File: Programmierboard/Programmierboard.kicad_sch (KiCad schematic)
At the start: 37 parts, among them J1 Conn_01x10_Socket, J2 Conn_01x10_Socket, J3 Conn_01x10_Socket, J4 Conn_01x10_Socket, J5 DE9_Plug_MountingHoles, J6 Conn_01x10_Socket, J7 Conn_01x10_Socket, Q1 BC327, Q2 BC327, SW1 SW_SPDT, U1 AT89C2051-12P, U2 MAX202, U99 L7805

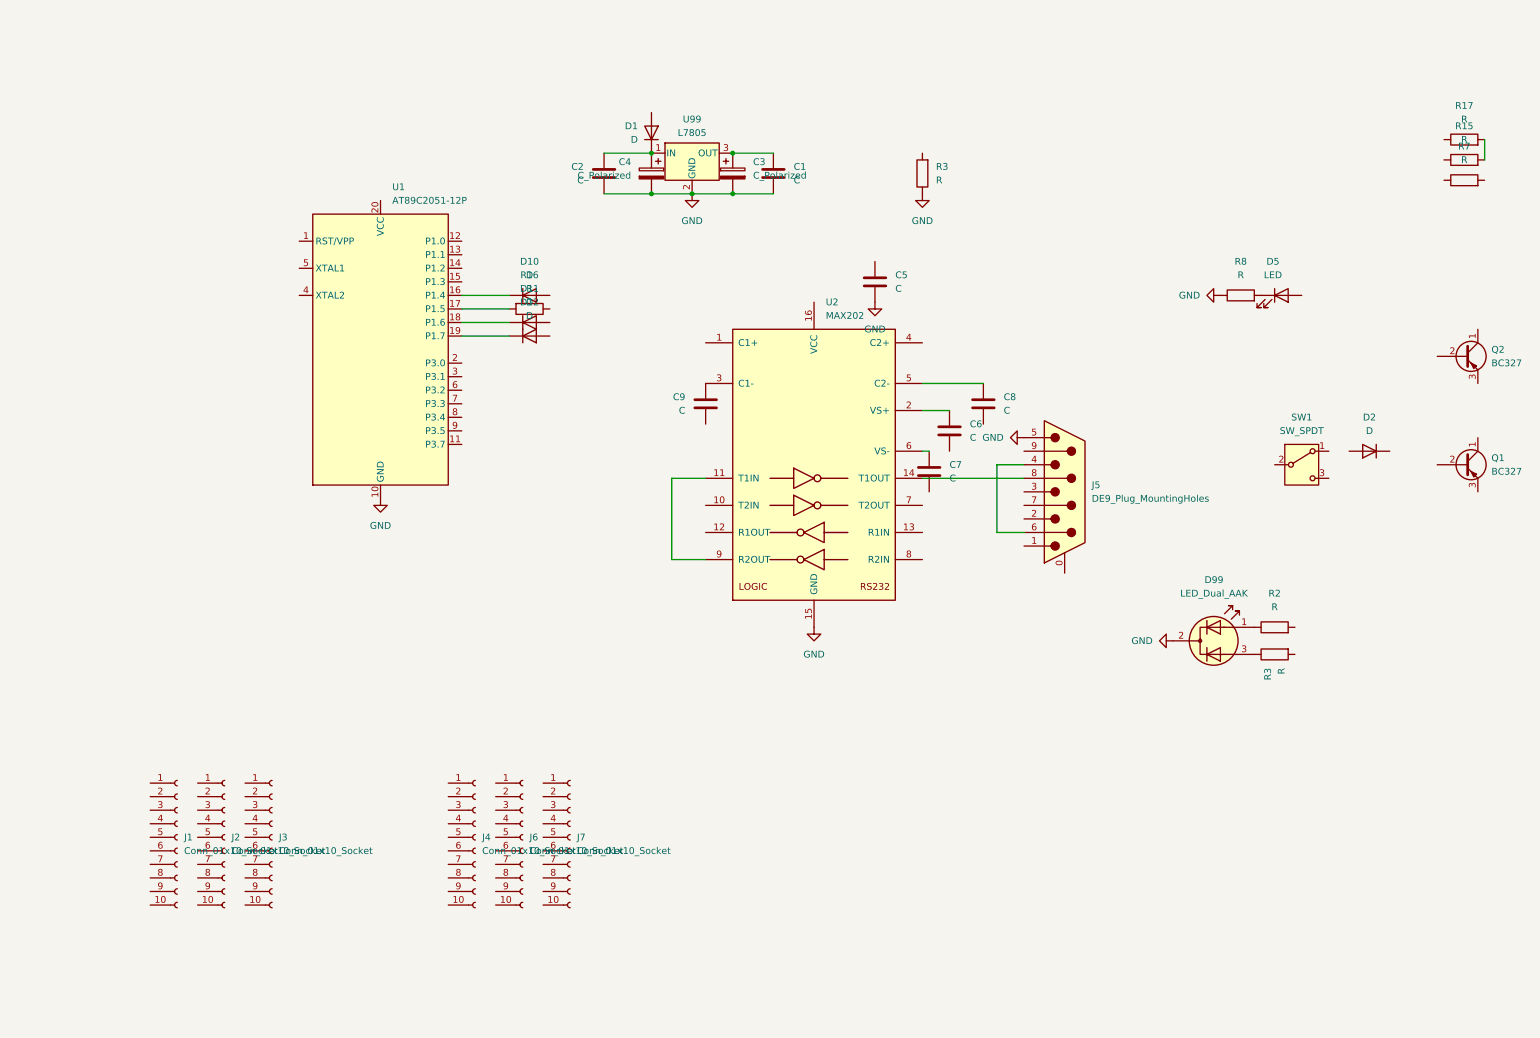
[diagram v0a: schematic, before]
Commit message: footprints und symbole
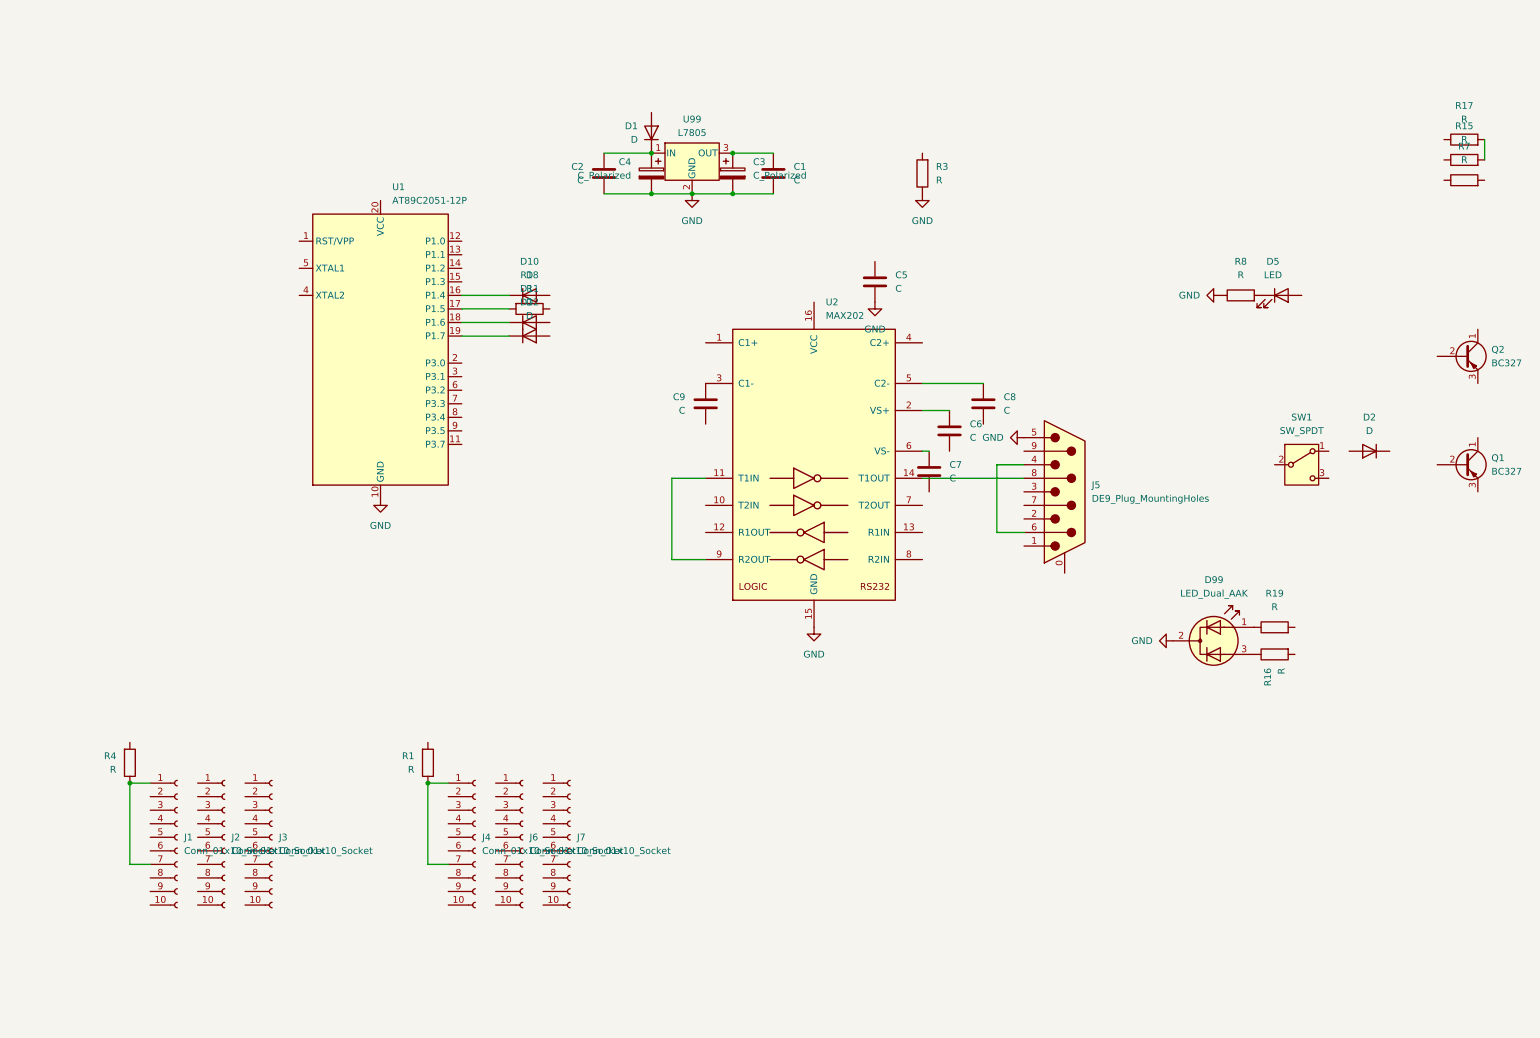
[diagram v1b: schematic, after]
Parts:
- added R1, R4: R, Resistor_THT:R_Axial_DIN0207_L6.3mm_D2.5mm_P10.16mm_Horizontal, symbol Device:R
- renumbered R3 to R16, R16 to R18, R2 to R19
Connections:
- net at J1.1 (Pin_1): now also J1.7 (Pin_7), R4.1
- net at J4.1 (Pin_1): now also J4.7 (Pin_7), R1.1
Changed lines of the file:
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@@
 	)
 	(junction
+		(at 22.86 160.02)
+		(diameter 0)
+		(color 0 0 0 0)
+	)
+	(junction
 		(at 135.89 49.53)
 		(diameter 0)
@@
 	)
 	(junction
+		(at 78.74 160.02)
+		(diameter 0)
+		(color 0 0 0 0)
+	)
+	(junction
 		(at 128.27 49.53)
 		(diameter 0)
@@
 	(wire
 		(pts
+			(xy 22.86 160.02) (xy 26.67 160.02)
+		)
+		(stroke
+			(width 0)
+			(type default)
+		)
+	)
+	(wire
+		(pts
+			(xy 82.55 175.26) (xy 78.74 175.26)
+		)
+		(stroke
+			(width 0)
+			(type default)
+		)
+	)
+	(wire
+		(pts
+			(xy 78.74 175.26) (xy 78.74 160.02)
+		)
+		(stroke
+			(width 0)
+			(type default)
+		)
+	)
+	(wire
+		(pts
 			(xy 124.46 118.11) (xy 124.46 102.87)
 		)
@@
 	(wire
 		(pts
+			(xy 78.74 160.02) (xy 82.55 160.02)
+		)
+		(stroke
+			(width 0)
+			(type default)
+		)
+	)
+	(wire
+		(pts
+			(xy 22.86 175.26) (xy 26.67 175.26)
+		)
+		(stroke
+			(width 0)
+			(type default)
+		)
+	)
+	(wire
+		(pts
 			(xy 85.09 73.66) (xy 93.98 73.66)
 		)
@@
 	(wire
 		(pts
+			(xy 22.86 160.02) (xy 22.86 175.26)
+		)
+		(stroke
+			(width 0)
+			(type default)
+		)
+	)
+	(wire
+		(pts
 			(xy 135.89 49.53) (xy 143.51 49.53)
 		)
@@
 		(dnp no)
 		(fields_autoplaced yes)
-		(property "Reference" "R16"
+		(property "Reference" "R18"
 			(at 97.79 64.77 90)
 			(effects
@@
 			(project "Programmierboard"
 				(path "/7a1d40ec-943a-4f9e-8e53-fdc73602617f"
-					(reference "R16")
+					(reference "R18")
 					(unit 1)
 				)
@@
 	)
 	(symbol
+		(lib_id "Device:R")
+		(at 78.74 156.21 0)
+		(mirror x)
+		(unit 1)
+		(exclude_from_sim no)
+		(in_bom yes)
+		(on_board yes)
+		(dnp no)
+		(property "Reference" "R1"
+			(at 76.2 154.9399 0)
+			(effects
+				(font
+					(size 1.27 1.27)
+				)
+				(justify right)
+			)
+		)
+		(property "Value" "R"
+			(at 76.2 157.4799 0)
+			(effects
+				(font
+					(size 1.27 1.27)
+				)
+				(justify right)
+			)
+		)
+		(property "Footprint" "Resistor_THT:R_Axial_DIN0207_L6.3mm_D2.5mm_P10.16mm_Horizontal"
+			(at 76.962 156.21 90)
+			(effects
+				(font
+					(size 1.27 1.27)
+				)
+				(hide yes)
+			)
+		)
+		(property "Datasheet" "~"
+			(at 78.74 156.21 0)
+			(effects
+				(font
+					(size 1.27 1.27)
+				)
+				(hide yes)
+			)
+		)
+		(property "Description" "Resistor"
+			(at 78.74 156.21 0)
+			(effects
+				(font
+					(size 1.27 1.27)
+				)
+				(hide yes)
+			)
+		)
+		(pin "2"
+		)
+		(pin "1"
+		)
+		(instances
+			(project "Programmierboard"
+				(path "/7a1d40ec-943a-4f9e-8e53-fdc73602617f"
+					(reference "R1")
+					(unit 1)
+				)
+			)
+		)
+	)
+	(symbol
 		(lib_id "Device:C")
 		(at 172.72 101.6 0)
@@
 	)
 	(symbol
+		(lib_id "Device:R")
+		(at 22.86 156.21 0)
+		(mirror x)
+		(unit 1)
+		(exclude_from_sim no)
+		(in_bom yes)
+		(on_board yes)
+		(dnp no)
+		(property "Reference" "R4"
+			(at 20.32 154.9399 0)
+			(effects
+				(font
+					(size 1.27 1.27)
+				)
+				(justify right)
+			)
+		)
+		(property "Value" "R"
+			(at 20.32 157.4799 0)
+			(effects
+				(font
+					(size 1.27 1.27)
+				)
+				(justify right)
+			)
+		)
+		(property "Footprint" "Resistor_THT:R_Axial_DIN0207_L6.3mm_D2.5mm_P10.16mm_Horizontal"
+			(at 21.082 156.21 90)
+			(effects
+				(font
+					(size 1.27 1.27)
+				)
+				(hide yes)
+			)
+		)
+		(property "Datasheet" "~"
+			(at 22.86 156.21 0)
+			(effects
+				(font
+					(size 1.27 1.27)
+				)
+				(hide yes)
+			)
+		)
+		(property "Description" "Resistor"
+			(at 22.86 156.21 0)
+			(effects
+				(font
+					(size 1.27 1.27)
+				)
+				(hide yes)
+			)
+		)
+		(pin "2"
+		)
+		(pin "1"
+		)
+		(instances
+			(project "Programmierboard"
+				(path "/7a1d40ec-943a-4f9e-8e53-fdc73602617f"
+					(reference "R4")
+					(unit 1)
+				)
+			)
+		)
+	)
+	(symbol
 		(lib_id "Transistor_BJT:BC327")
 		(at 273.05 80.01 0)
@@
 		(dnp no)
 		(fields_autoplaced yes)
-		(property "Reference" "R2"
+		(property "Reference" "R19"
 			(at 237.49 124.46 90)
 			(effects
@@
 			(project "Programmierboard"
 				(path "/7a1d40ec-943a-4f9e-8e53-fdc73602617f"
-					(reference "R2")
+					(reference "R19")
 					(unit 1)
 				)
@@
 		(on_board yes)
 		(dnp no)
-		(property "Reference" "R3"
+		(property "Reference" "R16"
 			(at 236.2199 138.43 0)
 			(effects
@@
 			(project "Programmierboard"
 				(path "/7a1d40ec-943a-4f9e-8e53-fdc73602617f"
-					(reference "R3")
+					(reference "R16")
 					(unit 1)
 				)

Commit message: prog
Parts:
- added C10: C, Capacitor_THT:C_Axial_L3.8mm_D2.6mm_P7.50mm_Horizontal, symbol Device:C
- added J8: Conn_01x02_Socket, Connector_PinSocket_2.54mm:PinSocket_1x02_P2.54mm_Vertical, symbol Connector:Conn_01x02_Socket
- D5: value LED -> POWER
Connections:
- net GND: now also C6.2, C7.2, C10.2, J8.2 (Pin_2)
- net VCC: now reaches U1.20 (VCC)
- net VCC: now also C1.1, C3.1, D5.2 (A), R1.2, R15.2, R17.2, U99.3 (OUT), C10.1
- net at J1.1 (Pin_1), J1.7 (Pin_7), R4.1: now also C5.1, J4.1 (Pin_1), J4.7 (Pin_7), R1.1
- new net +12V: J8.1 (Pin_1)
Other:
- moved on the sheet: C5, R17

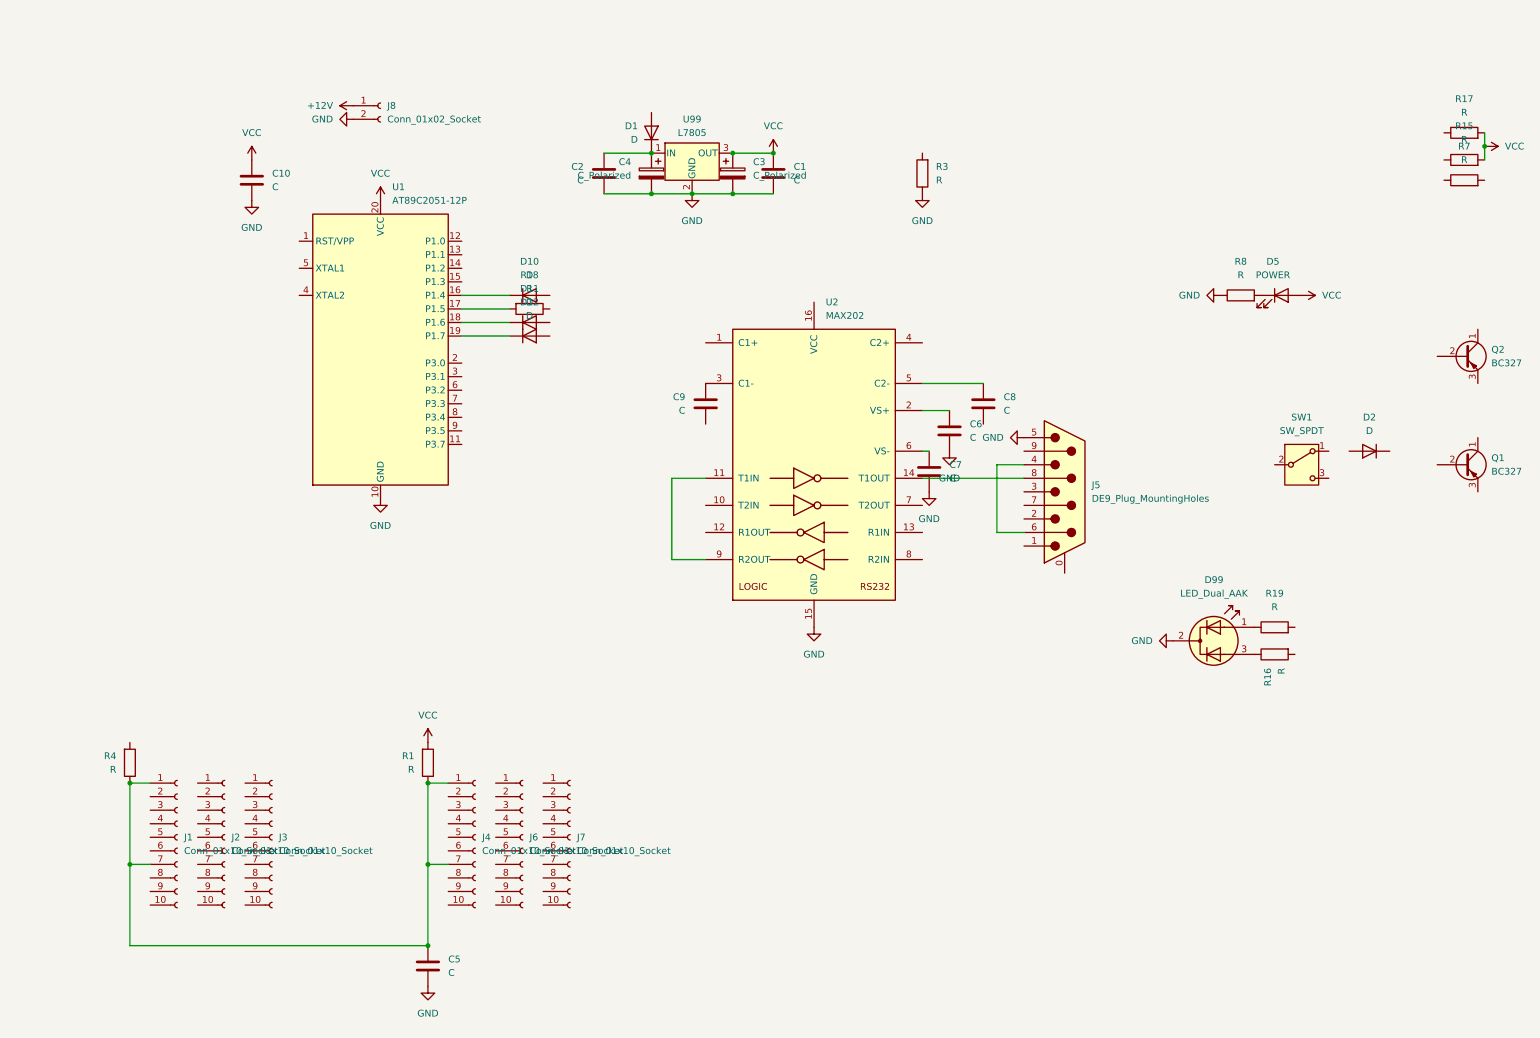
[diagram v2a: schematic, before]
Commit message: programmierboard bis auf 2 linien
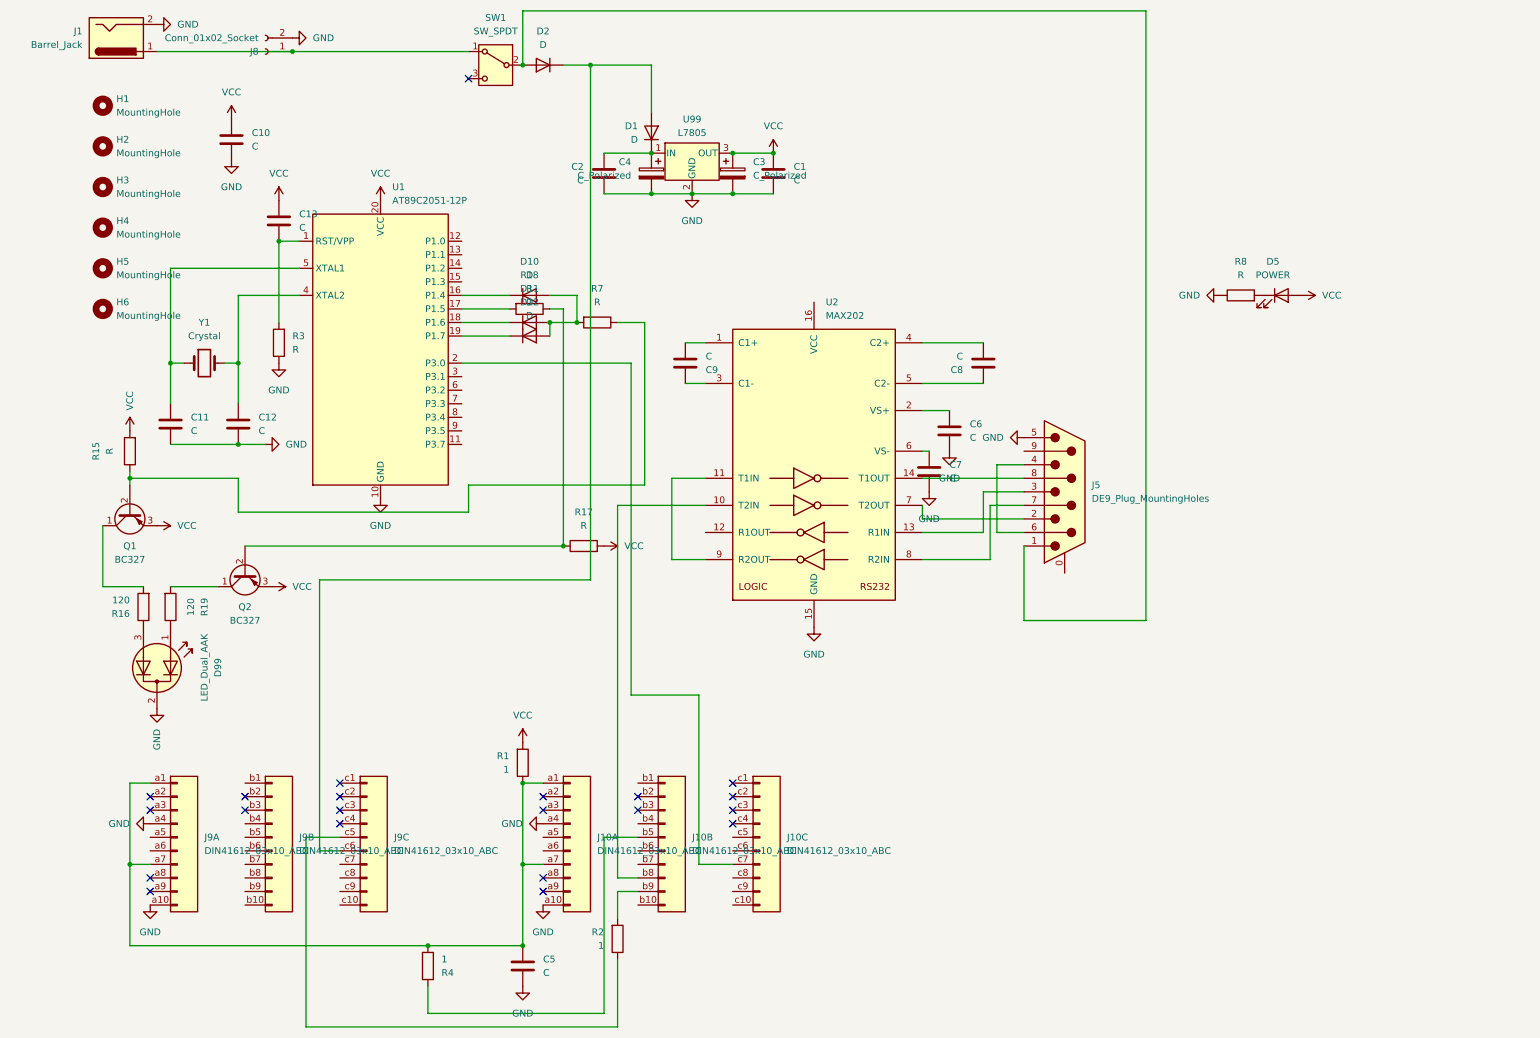
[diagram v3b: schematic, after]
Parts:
- removed J1, J2, J3, J4, J6, J7: Conn_01x10_Socket, Connector_PinSocket_2.54mm:PinSocket_1x10_P2.54mm_Vertical, symbol Connector:Conn_01x10_Socket
- added C11, C12: C, Capacitor_THT:C_Disc_D4.3mm_W1.9mm_P5.00mm, symbol Device:C
- added C13: C, Capacitor_THT:CP_Radial_Tantal_D4.5mm_P2.50mm, symbol Device:C
- added H1, H2, H3, H4, H5, H6: MountingHole, MountingHole:MountingHole_3.2mm_M3_DIN965, symbol Mechanical:MountingHole
- added J1: Barrel_Jack, Connector_BarrelJack:BarrelJack_SwitchcraftConxall_RAPC10U_Horizontal, symbol Connector:Barrel_Jack
- added J10, J9: DIN41612_03x10_ABC, Connector_DIN:DIN41612_C3_3x10_Female_Vertical_THT, symbol DIN41612:DIN41612_03x10_ABC
- added R2: 1, Resistor_THT:R_Axial_DIN0207_L6.3mm_D2.5mm_P10.16mm_Horizontal, symbol Device:R
- added Y1: Crystal, Crystal:Crystal_HC18-U_Vertical, symbol Device:Crystal
- J5: footprint Connector_Dsub:DSUB-9_Female_Horizontal_P2.77x2.84mm_EdgePinOffset4.94mm_Housed_MountingHolesOffset7.48mm -> Connector_Dsub:DSUB-9_Socket_Horizontal_P2.77x2.84mm_EdgePinOffset7.70mm_Housed_MountingHolesOffset9.12mm
- Q1, Q2: footprint Package_TO_SOT_THT:TO-92_Inline -> Package_TO_SOT_THT:TO-92
- R1, R4: value R -> 1
- R16, R19: value R -> 120
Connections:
- net +12V is gone; now on an unnamed net: J8.1 (Pin_1)
- net GND: now also C11.2, C12.2, J1.2, J10.a10 (Pin_a10), J10.a4 (Pin_a4), J9.a10 (Pin_a10), J9.a4 (Pin_a4)
- net VCC: now also Q1.3 (E), Q2.3 (E), C13.1
- net at C9.2: now also U2.1 (C1+)
- net at U1.1 (RST/VPP): now also R3.2, C13.2
- net at U1.2 (P3.0): now also J10.c7 (Pin_c7)
- net at U1.4 (XTAL2): now also C12.1, Y1.2
- net at U1.5 (XTAL1): now also C11.1, Y1.1
- net at J5.1: now also D2.2 (A), SW1.2 (B)
- net at J5.2: now also U2.7 (T2OUT)
- net at J5.3: now also U2.13 (R1IN)
- net at J5.7: now also U2.8 (R2IN)
- net at R18.1: now also Q2.2 (B), R17.1
- net at D1.2 (A): now also D2.1 (K), J9.c6 (Pin_c6)
- net at C5.1, R1.1, R4.1: now also J10.a1 (Pin_a1), J10.a7 (Pin_a7), J9.a1 (Pin_a1), J9.a7 (Pin_a7)
- net at R4.2: now also J10.b5 (Pin_b5)
- net at Q2.1 (C): now also R19.2
- net at SW1.1 (A): now also J1.1
- net at D10.2 (A): now also D11.2 (A), D12.2 (A), R7.2
- net at R7.1: now also Q1.2 (B), R15.1
- net at C8.2: now also U2.4 (C2+)
- net at U2.10 (T2IN): now also J10.b8 (Pin_b8)
- net at Q1.1 (C): now also R16.2
- new net: J9.c5 (Pin_c5), R2.1
- new net: J10.b9 (Pin_b9), R2.2
- no-connect marks 0 -> 21
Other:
- moved on the sheet: C10, C5, C8, C9, D2, D99, J8, Q1, Q2, R1, R15, R16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
